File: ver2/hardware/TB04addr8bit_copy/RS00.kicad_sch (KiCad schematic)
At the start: 20 parts, among them IC201 74HC161N, IC202 74HC161N, IC203 74HC161N, IC204 74HC161N, J201 Conn_02x05_Odd_Even, J202 Conn_02x05_Odd_Even, J203 Conn_02x05_Odd_Even, J204 Conn_02x05_Odd_Even, U201 74LS253, U202 74LS253, U203 74LS253, U204 74LS253

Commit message: ver2: ロータリースイッチSR1712F-0109のフットプリントを作成／SW502をrotarySW_01x09へ差し替え
- データシート(SLH-232)の埋め込み画像を読み、穴位置を実測して寸法を確定
  端子10-Ø0.9(2列×5・ピッチ2.5・列間18.3)、取付2-Ø2.0(間隔16.0・中点から1.1)
- KiCAD標準のSW_Rotary_1x9_MPは実物とピン番号が逆(pin10がコモン)だったため
  My_Lib:rotarySW_01x09(pin1=コモン)へ差し替え。実物・シンボル・FPが三者一致
- pcbnewのAPIでパッド12個の座標を全数検証
- マスターにfp-lib-tableを追加(footprints/Library.pretty)

Co-Authored-By: Claude Opus 5 <noreply@anthropic.com>
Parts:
- J201, J202, J203, J204: footprint (none) -> Connector_PinSocket_2.54mm:PinSocket_2x05_P2.54mm_Vertical
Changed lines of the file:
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@@
 		)
 		(instances
-			(project "TB04addr8bit"
+			(project "TB04addr8bit_copy"
 				(path "/d176c79b-dced-4d01-bcec-7dfd676fcfc2/a1fb1557-9779-47a0-87e0-44b80b522f7b"
 					(reference "U202")
@@
 		)
 		(instances
-			(project "TB04addr8bit"
+			(project "TB04addr8bit_copy"
 				(path "/d176c79b-dced-4d01-bcec-7dfd676fcfc2/a1fb1557-9779-47a0-87e0-44b80b522f7b"
 					(reference "C206")
@@
 		)
 		(instances
-			(project "TB04addr8bit"
+			(project "TB04addr8bit_copy"
 				(path "/d176c79b-dced-4d01-bcec-7dfd676fcfc2/a1fb1557-9779-47a0-87e0-44b80b522f7b"
 					(reference "#PWR0214")
@@
 		)
 		(instances
-			(project "TB04addr8bit"
+			(project "TB04addr8bit_copy"
 				(path "/d176c79b-dced-4d01-bcec-7dfd676fcfc2/a1fb1557-9779-47a0-87e0-44b80b522f7b"
 					(reference "C208")
@@
 		)
 		(instances
-			(project "TB04addr8bit"
+			(project "TB04addr8bit_copy"
 				(path "/d176c79b-dced-4d01-bcec-7dfd676fcfc2/a1fb1557-9779-47a0-87e0-44b80b522f7b"
 					(reference "C203")
@@
 		)
 		(instances
-			(project "TB04addr8bit"
+			(project "TB04addr8bit_copy"
 				(path "/d176c79b-dced-4d01-bcec-7dfd676fcfc2/a1fb1557-9779-47a0-87e0-44b80b522f7b"
 					(reference "#PWR0202")
@@
 		)
 		(instances
-			(project "TB04addr8bit"
+			(project "TB04addr8bit_copy"
 				(path "/d176c79b-dced-4d01-bcec-7dfd676fcfc2/a1fb1557-9779-47a0-87e0-44b80b522f7b"
 					(reference "C207")
@@
 		)
 		(instances
-			(project "TB04addr8bit"
+			(project "TB04addr8bit_copy"
 				(path "/d176c79b-dced-4d01-bcec-7dfd676fcfc2/a1fb1557-9779-47a0-87e0-44b80b522f7b"
 					(reference "U203")
@@
 		)
 		(instances
-			(project "TB04addr8bit"
+			(project "TB04addr8bit_copy"
 				(path "/d176c79b-dced-4d01-bcec-7dfd676fcfc2/a1fb1557-9779-47a0-87e0-44b80b522f7b"
 					(reference "U204")
@@
 		)
 		(instances
-			(project "TB04addr8bit"
+			(project "TB04addr8bit_copy"
 				(path "/d176c79b-dced-4d01-bcec-7dfd676fcfc2/a1fb1557-9779-47a0-87e0-44b80b522f7b"
 					(reference "IC202")
@@
 		)
 		(instances
-			(project "TB04addr8bit"
+			(project "TB04addr8bit_copy"
 				(path "/d176c79b-dced-4d01-bcec-7dfd676fcfc2/a1fb1557-9779-47a0-87e0-44b80b522f7b"
 					(reference "C205")
@@
 		)
 		(instances
-			(project "TB04addr8bit"
+			(project "TB04addr8bit_copy"
 				(path "/d176c79b-dced-4d01-bcec-7dfd676fcfc2/a1fb1557-9779-47a0-87e0-44b80b522f7b"
 					(reference "C204")
@@
 		)
 		(instances
-			(project "TB04addr8bit"
+			(project "TB04addr8bit_copy"
 				(path "/d176c79b-dced-4d01-bcec-7dfd676fcfc2/a1fb1557-9779-47a0-87e0-44b80b522f7b"
 					(reference "#PWR0205")
@@
 		)
 		(instances
-			(project "TB04addr8bit"
+			(project "TB04addr8bit_copy"
 				(path "/d176c79b-dced-4d01-bcec-7dfd676fcfc2/a1fb1557-9779-47a0-87e0-44b80b522f7b"
 					(reference "#PWR0211")
@@
 		)
 		(instances
-			(project "TB04addr8bit"
+			(project "TB04addr8bit_copy"
 				(path "/d176c79b-dced-4d01-bcec-7dfd676fcfc2/a1fb1557-9779-47a0-87e0-44b80b522f7b"
 					(reference "C202")
@@
 		)
 		(instances
-			(project "TB04addr8bit"
+			(project "TB04addr8bit_copy"
 				(path "/d176c79b-dced-4d01-bcec-7dfd676fcfc2/a1fb1557-9779-47a0-87e0-44b80b522f7b"
 					(reference "#PWR0209")
@@
 		)
 		(instances
-			(project "TB04addr8bit"
+			(project "TB04addr8bit_copy"
 				(path "/d176c79b-dced-4d01-bcec-7dfd676fcfc2/a1fb1557-9779-47a0-87e0-44b80b522f7b"
 					(reference "#PWR0217")
@@
 		)
 		(instances
-			(project "TB04addr8bit"
+			(project "TB04addr8bit_copy"
 				(path "/d176c79b-dced-4d01-bcec-7dfd676fcfc2/a1fb1557-9779-47a0-87e0-44b80b522f7b"
 					(reference "#PWR0208")
@@
 		)
 		(instances
-			(project "TB04addr8bit"
+			(project "TB04addr8bit_copy"
 				(path "/d176c79b-dced-4d01-bcec-7dfd676fcfc2/a1fb1557-9779-47a0-87e0-44b80b522f7b"
 					(reference "#PWR0218")
@@
 			)
 		)
-		(property "Footprint" ""
+		(property "Footprint" "Connector_PinSocket_2.54mm:PinSocket_2x05_P2.54mm_Vertical"
 			(at 187.96 113.03 0)
 			(hide yes)
@@
 		)
 		(instances
-			(project "TB04addr8bit"
+			(project "TB04addr8bit_copy"
 				(path "/d176c79b-dced-4d01-bcec-7dfd676fcfc2/a1fb1557-9779-47a0-87e0-44b80b522f7b"
 					(reference "J203")
@@
 		)
 		(instances
-			(project "TB04addr8bit"
+			(project "TB04addr8bit_copy"
 				(path "/d176c79b-dced-4d01-bcec-7dfd676fcfc2/a1fb1557-9779-47a0-87e0-44b80b522f7b"
 					(reference "#PWR0207")
@@
 		)
 		(instances
-			(project "TB04addr8bit"
+			(project "TB04addr8bit_copy"
 				(path "/d176c79b-dced-4d01-bcec-7dfd676fcfc2/a1fb1557-9779-47a0-87e0-44b80b522f7b"
 					(reference "#PWR0212")
@@
 		)
 		(instances
-			(project "TB04addr8bit"
+			(project "TB04addr8bit_copy"
 				(path "/d176c79b-dced-4d01-bcec-7dfd676fcfc2/a1fb1557-9779-47a0-87e0-44b80b522f7b"
 					(reference "#PWR0213")
@@
 		)
 		(instances
-			(project "TB04addr8bit"
+			(project "TB04addr8bit_copy"
 				(path "/d176c79b-dced-4d01-bcec-7dfd676fcfc2/a1fb1557-9779-47a0-87e0-44b80b522f7b"
 					(reference "#PWR0204")
@@
 		)
 		(instances
-			(project "TB04addr8bit"
+			(project "TB04addr8bit_copy"
 				(path "/d176c79b-dced-4d01-bcec-7dfd676fcfc2/a1fb1557-9779-47a0-87e0-44b80b522f7b"
 					(reference "#PWR0216")
@@
 		)
 		(instances
-			(project "TB04addr8bit"
+			(project "TB04addr8bit_copy"
 				(path "/d176c79b-dced-4d01-bcec-7dfd676fcfc2/a1fb1557-9779-47a0-87e0-44b80b522f7b"
 					(reference "IC204")
@@
 		)
 		(instances
-			(project "TB04addr8bit"
+			(project "TB04addr8bit_copy"
 				(path "/d176c79b-dced-4d01-bcec-7dfd676fcfc2/a1fb1557-9779-47a0-87e0-44b80b522f7b"
 					(reference "IC203")
@@
 		)
 		(instances
-			(project "TB04addr8bit"
+			(project "TB04addr8bit_copy"
 				(path "/d176c79b-dced-4d01-bcec-7dfd676fcfc2/a1fb1557-9779-47a0-87e0-44b80b522f7b"
 					(reference "#PWR0220")
@@
 		)
 		(instances
-			(project "TB04addr8bit"
+			(project "TB04addr8bit_copy"
 				(path "/d176c79b-dced-4d01-bcec-7dfd676fcfc2/a1fb1557-9779-47a0-87e0-44b80b522f7b"
 					(reference "#PWR0219")
@@
 		)
 		(instances
-			(project "TB04addr8bit"
+			(project "TB04addr8bit_copy"
 				(path "/d176c79b-dced-4d01-bcec-7dfd676fcfc2/a1fb1557-9779-47a0-87e0-44b80b522f7b"
 					(reference "#PWR0203")
@@
 		)
 		(instances
-			(project "TB04addr8bit"
+			(project "TB04addr8bit_copy"
 				(path "/d176c79b-dced-4d01-bcec-7dfd676fcfc2/a1fb1557-9779-47a0-87e0-44b80b522f7b"
 					(reference "#PWR0206")
@@
 		)
 		(instances
-			(project "TB04addr8bit"
+			(project "TB04addr8bit_copy"
 				(path "/d176c79b-dced-4d01-bcec-7dfd676fcfc2/a1fb1557-9779-47a0-87e0-44b80b522f7b"
 					(reference "#PWR0210")
@@
 		)
 		(instances
-			(project "TB04addr8bit"
+			(project "TB04addr8bit_copy"
 				(path "/d176c79b-dced-4d01-bcec-7dfd676fcfc2/a1fb1557-9779-47a0-87e0-44b80b522f7b"
 					(reference "#PWR0201")
@@
 		)
 		(instances
-			(project "TB04addr8bit"
+			(project "TB04addr8bit_copy"
 				(path "/d176c79b-dced-4d01-bcec-7dfd676fcfc2/a1fb1557-9779-47a0-87e0-44b80b522f7b"
 					(reference "#PWR0215")
@@
 			)
 		)
-		(property "Footprint" ""
+		(property "Footprint" "Connector_PinSocket_2.54mm:PinSocket_2x05_P2.54mm_Vertical"
 			(at 208.28 53.34 0)
 			(hide yes)
@@
 		)
 		(instances
-			(project "TB04addr8bit"
+			(project "TB04addr8bit_copy"
 				(path "/d176c79b-dced-4d01-bcec-7dfd676fcfc2/a1fb1557-9779-47a0-87e0-44b80b522f7b"
 					(reference "J201")
@@
 		)
 		(instances
-			(project "TB04addr8bit"
+			(project "TB04addr8bit_copy"
 				(path "/d176c79b-dced-4d01-bcec-7dfd676fcfc2/a1fb1557-9779-47a0-87e0-44b80b522f7b"
 					(reference "IC201")
@@
 		)
 		(instances
-			(project "TB04addr8bit"
+			(project "TB04addr8bit_copy"
 				(path "/d176c79b-dced-4d01-bcec-7dfd676fcfc2/a1fb1557-9779-47a0-87e0-44b80b522f7b"
 					(reference "C201")
@@
 			)
 		)
-		(property "Footprint" ""
+		(property "Footprint" "Connector_PinSocket_2.54mm:PinSocket_2x05_P2.54mm_Vertical"
 			(at 158.75 64.77 0)
 			(hide yes)
@@
 		)
 		(instances
-			(project "TB04addr8bit"
+			(project "TB04addr8bit_copy"
 				(path "/d176c79b-dced-4d01-bcec-7dfd676fcfc2/a1fb1557-9779-47a0-87e0-44b80b522f7b"
 					(reference "J202")
@@
 		)
 		(instances
-			(project "TB04addr8bit"
+			(project "TB04addr8bit_copy"
 				(path "/d176c79b-dced-4d01-bcec-7dfd676fcfc2/a1fb1557-9779-47a0-87e0-44b80b522f7b"
 					(reference "U201")
@@
 			)
 		)
-		(property "Footprint" ""
+		(property "Footprint" "Connector_PinSocket_2.54mm:PinSocket_2x05_P2.54mm_Vertical"
 			(at 143.51 163.83 0)
 			(hide yes)
@@
 		)
 		(instances
-			(project "TB04addr8bit"
+			(project "TB04addr8bit_copy"
 				(path "/d176c79b-dced-4d01-bcec-7dfd676fcfc2/a1fb1557-9779-47a0-87e0-44b80b522f7b"
 					(reference "J204")

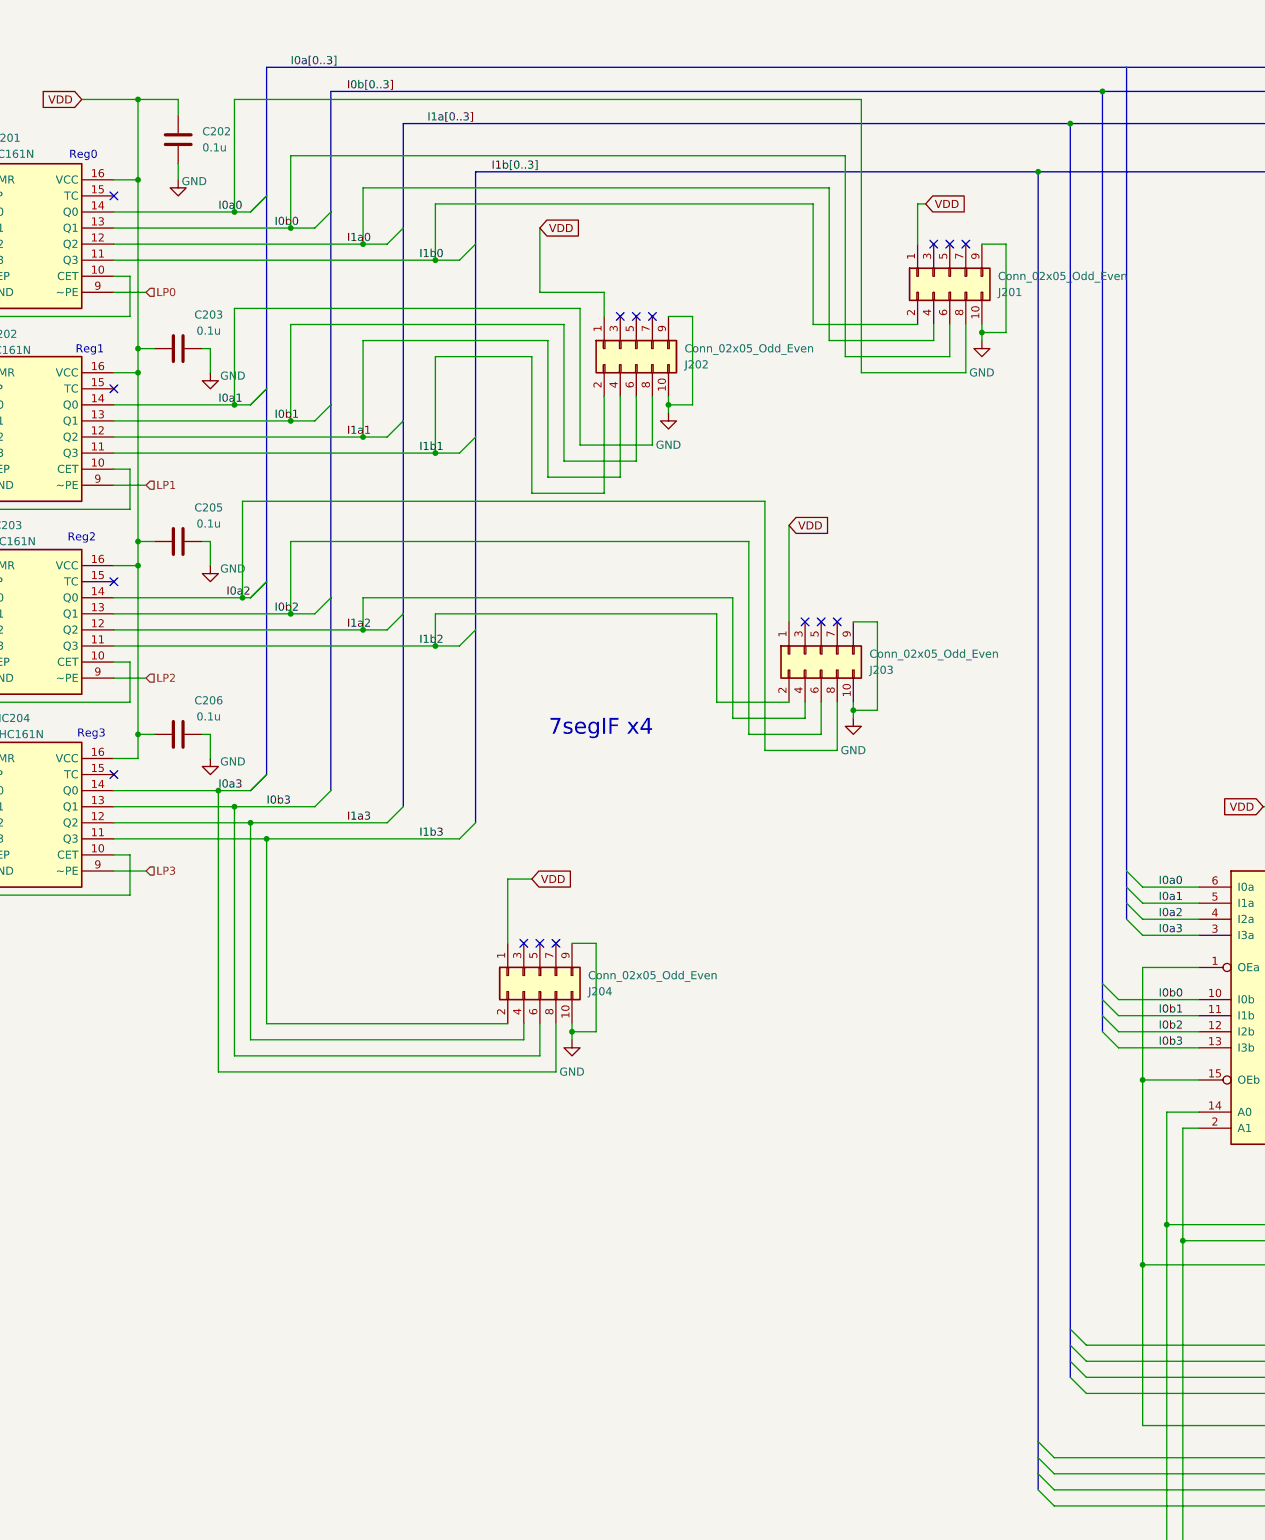
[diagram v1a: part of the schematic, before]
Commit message: ver2: レジスタLED32個を追加し、それを織り込んでPCBを再配置
- 回路図にレジスタ表示LED(D2xx/D3xx)とSIP抵抗を追加(部品279→307)
- 密度は61.3%→62.4%でほぼ変わらず
- RS00/RS01を下端の帯の上に固定し、ブロック内でLEDを手前側へ
- 6xx/7xx/15xxを横長にして上部に収め、基板内14/16グループに改善
- 部品の重なり0・基板内281個/はみ出し26個

Co-Authored-By: Claude Opus 5 <noreply@anthropic.com>
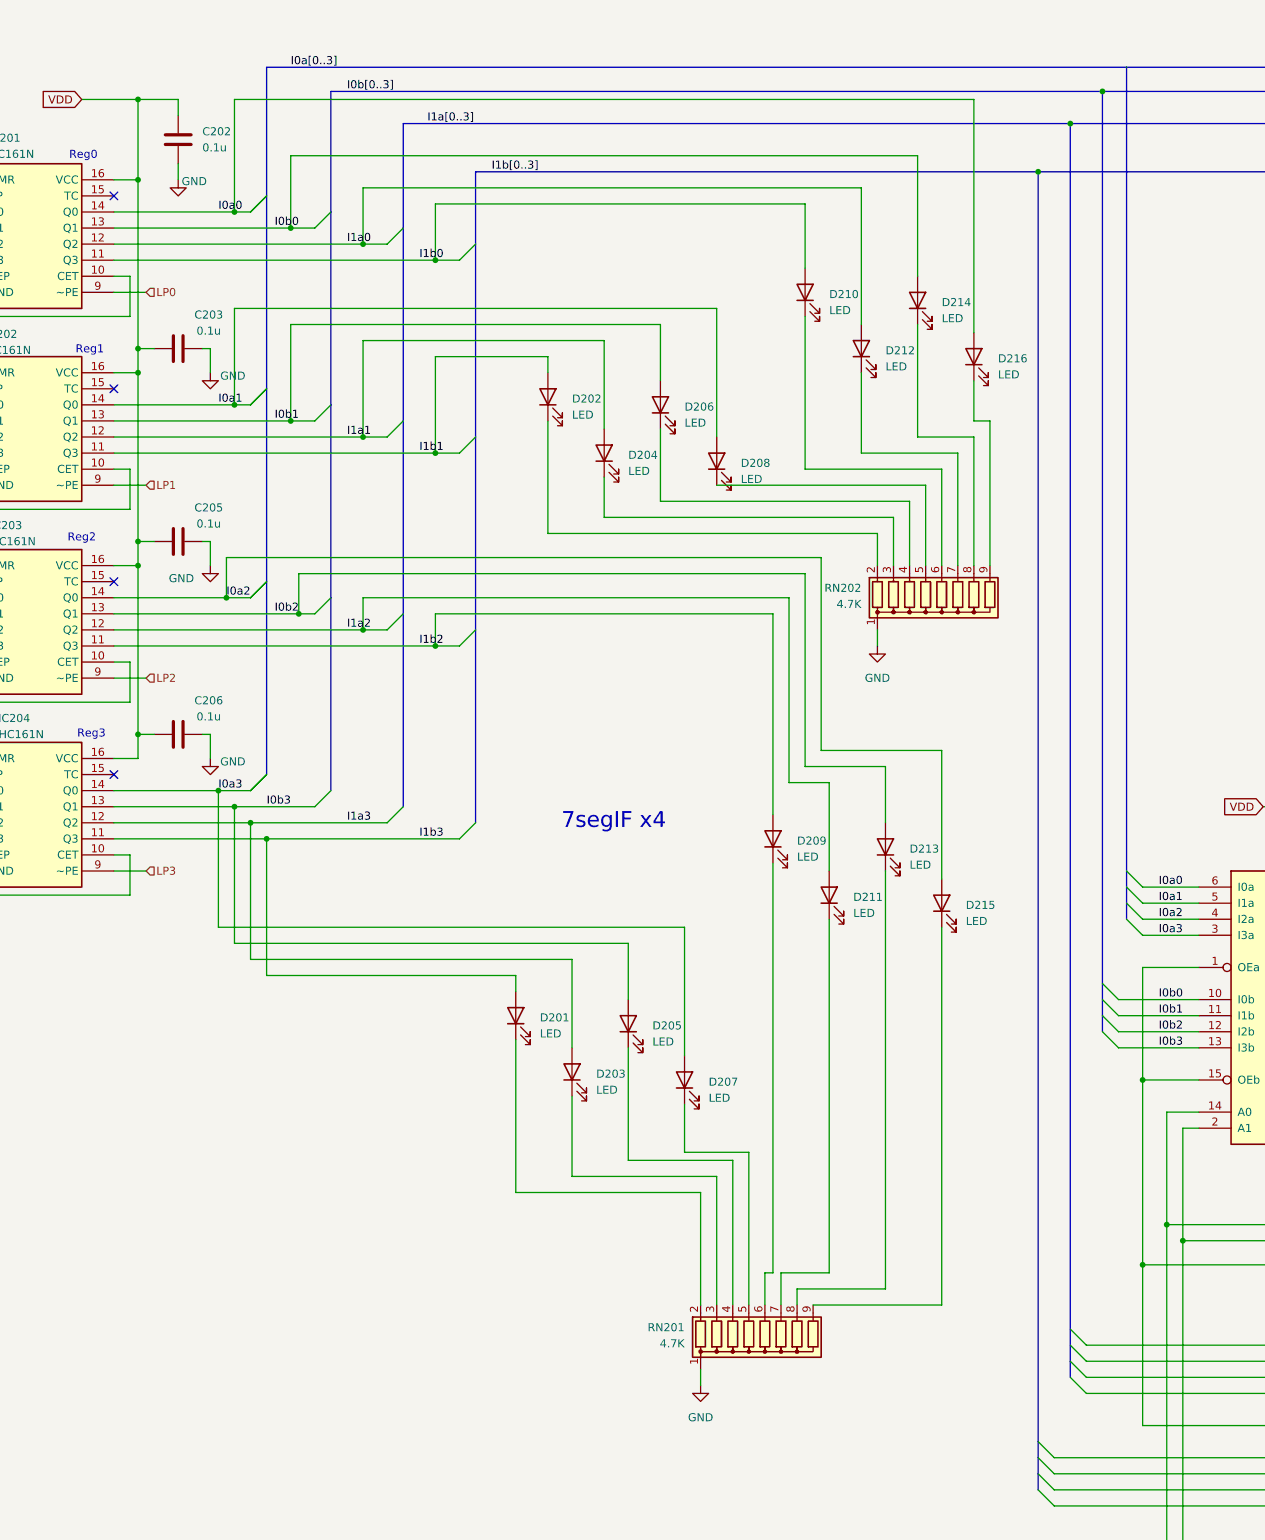
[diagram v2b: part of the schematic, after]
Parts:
- removed J201, J202, J203, J204: Conn_02x05_Odd_Even, Connector_PinSocket_2.54mm:PinSocket_2x05_P2.54mm_Vertical, symbol Connector_Generic:Conn_02x05_Odd_Even
- added D201, D202, D203, D204, D205, D206, D207, D208, D209, D210, D211, D212, D213, D214, D215, D216: LED, LED_THT:LED_D3.0mm_Clear, symbol Device:LED
- added RN201, RN202: 4.7K, Resistor_THT:R_Array_SIP9, symbol Device:R_Network08
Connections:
- net GND: now also RN201.1 (common), RN202.1 (common)
- net I0a0: now also D216.2 (A)
- net I0a1: now also D208.2 (A)
- net I0a2: now also D215.2 (A)
- net I0a3: now also D207.2 (A)
- net I0b0: now also D214.2 (A)
- net I0b1: now also D206.2 (A)
- net I0b2: now also D213.2 (A)
- net I0b3: now also D205.2 (A)
- net I1a0: now also D212.2 (A)
- net I1a1: now also D204.2 (A)
- net I1a2: now also D211.2 (A)
- net I1a3: now also D203.2 (A)
- net I1b0: now also D210.2 (A)
- net I1b1: now also D202.2 (A)
- net I1b2: now also D209.2 (A)
- net I1b3: now also D201.2 (A)
- new net: D205.1 (K), RN201.4 (R3)
- new net: D208.1 (K), RN202.5 (R4)
- new net: D216.1 (K), RN202.9 (R8)
- new net: D215.1 (K), RN201.9 (R8)
- new net: D204.1 (K), RN202.3 (R2)
- new net: D207.1 (K), RN201.5 (R4)
- new net: D201.1 (K), RN201.2 (R1)
- new net: D214.1 (K), RN202.8 (R7)
- new net: D211.1 (K), RN201.7 (R6)
- new net: D209.1 (K), RN201.6 (R5)
- new net: D210.1 (K), RN202.6 (R5)
- new net: D202.1 (K), RN202.2 (R1)
- new net: D203.1 (K), RN201.3 (R2)
- new net: D206.1 (K), RN202.4 (R3)
- new net: D212.1 (K), RN202.7 (R6)
- new net: D213.1 (K), RN201.8 (R7)
- no-connect marks 16 -> 4

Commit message: ver2: 分割元TB04addr8bit_copyの74LS表記もHCへ(Valueのみ56件)
3分割と同じスクリプトを適用。置換56件は3分割の合計と一致。
副産物として、3分割の合計と_copyの品種別パッケージ数が全数一致
(253x12/161Nx11/244x10/273x6/157x4/377x4ほか計61)することを確認
= ICの取りこぼし・重複がないことの独立した裏づけ。

検証: 残存する74LSのValue 0件、変更行はValueの56行のみ
凍結マスターTB04addr8bitは08-23の状態で古いため対象外

Co-Authored-By: Claude Opus 5 <noreply@anthropic.com>
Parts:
- U201, U202, U203, U204: value 74LS253 -> 74HC253
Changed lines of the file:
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@@
 			)
 		)
-		(property "Value" "74LS253"
+		(property "Value" "74HC253"
 			(at 327.2633 99.06 0)
 			(show_name no)
@@
 			)
 		)
-		(property "Value" "74LS253"
+		(property "Value" "74HC253"
 			(at 262.4933 144.78 0)
 			(show_name no)
@@
 			)
 		)
-		(property "Value" "74LS253"
+		(property "Value" "74HC253"
 			(at 294.2433 217.17 0)
 			(show_name no)
@@
 			)
 		)
-		(property "Value" "74LS253"
+		(property "Value" "74HC253"
 			(at 327.2633 21.59 0)
 			(show_name no)
